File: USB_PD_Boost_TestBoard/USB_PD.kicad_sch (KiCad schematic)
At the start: 44 parts, among them IC1 CYPD3177-24LQXQ, Q1 SI7997DP-T1-GE3, Q2 SI7997DP-T1-GE3, Q3 IRLML0030

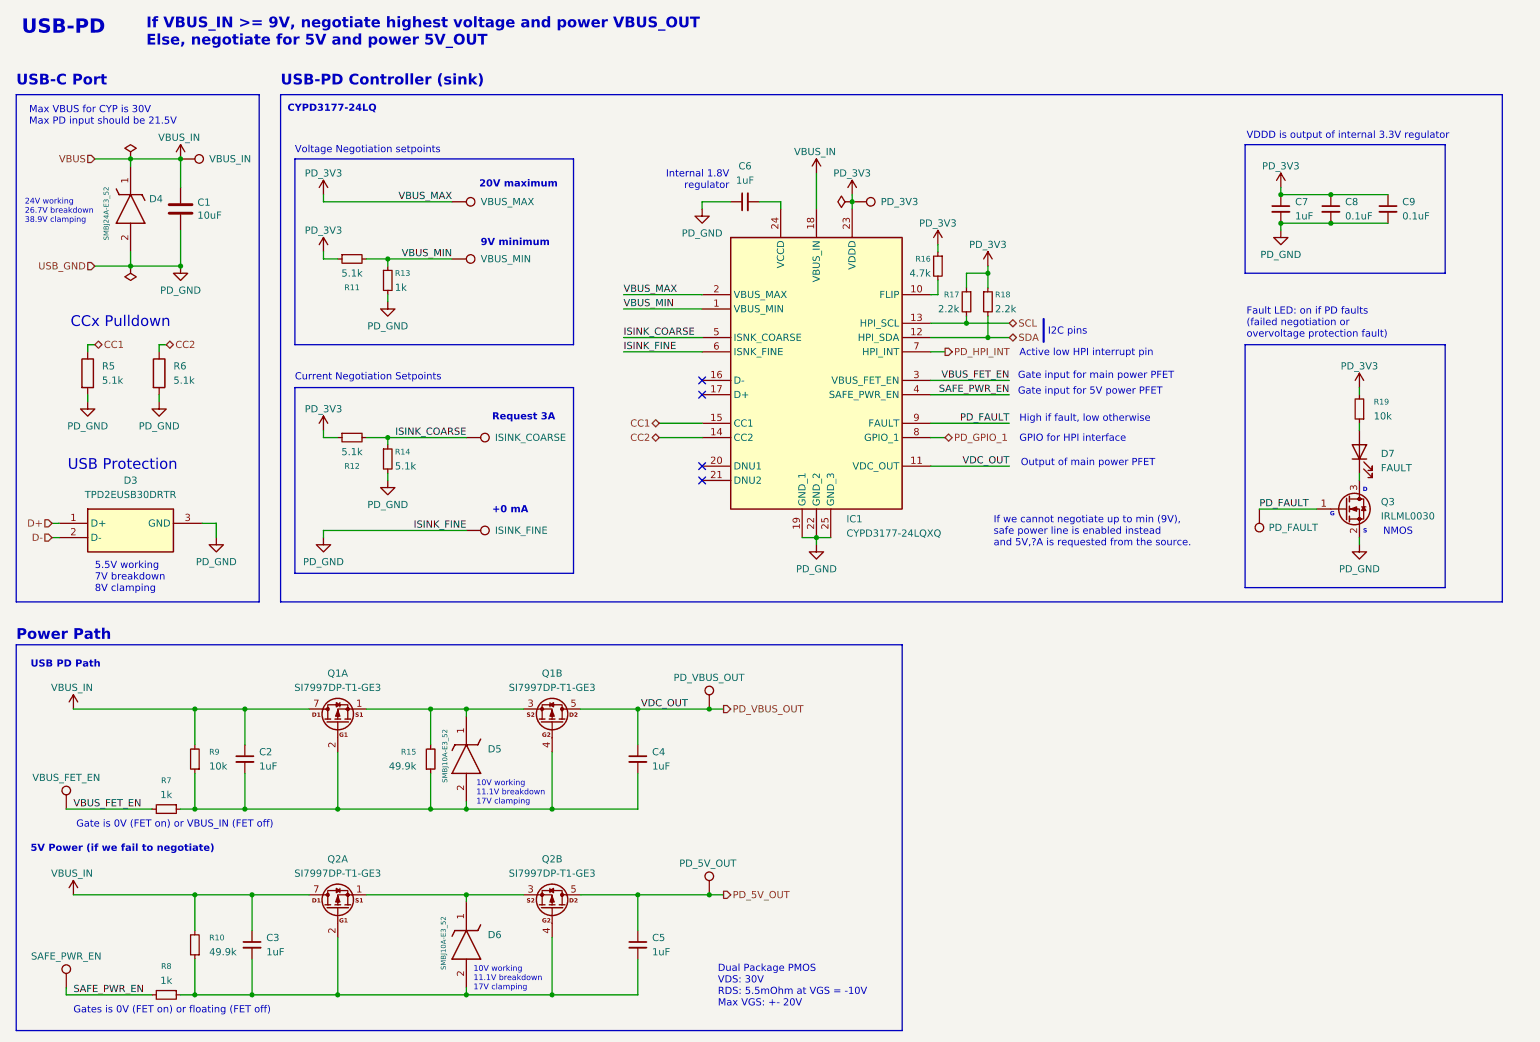
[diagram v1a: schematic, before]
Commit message: addressed comments, changed PD block a little
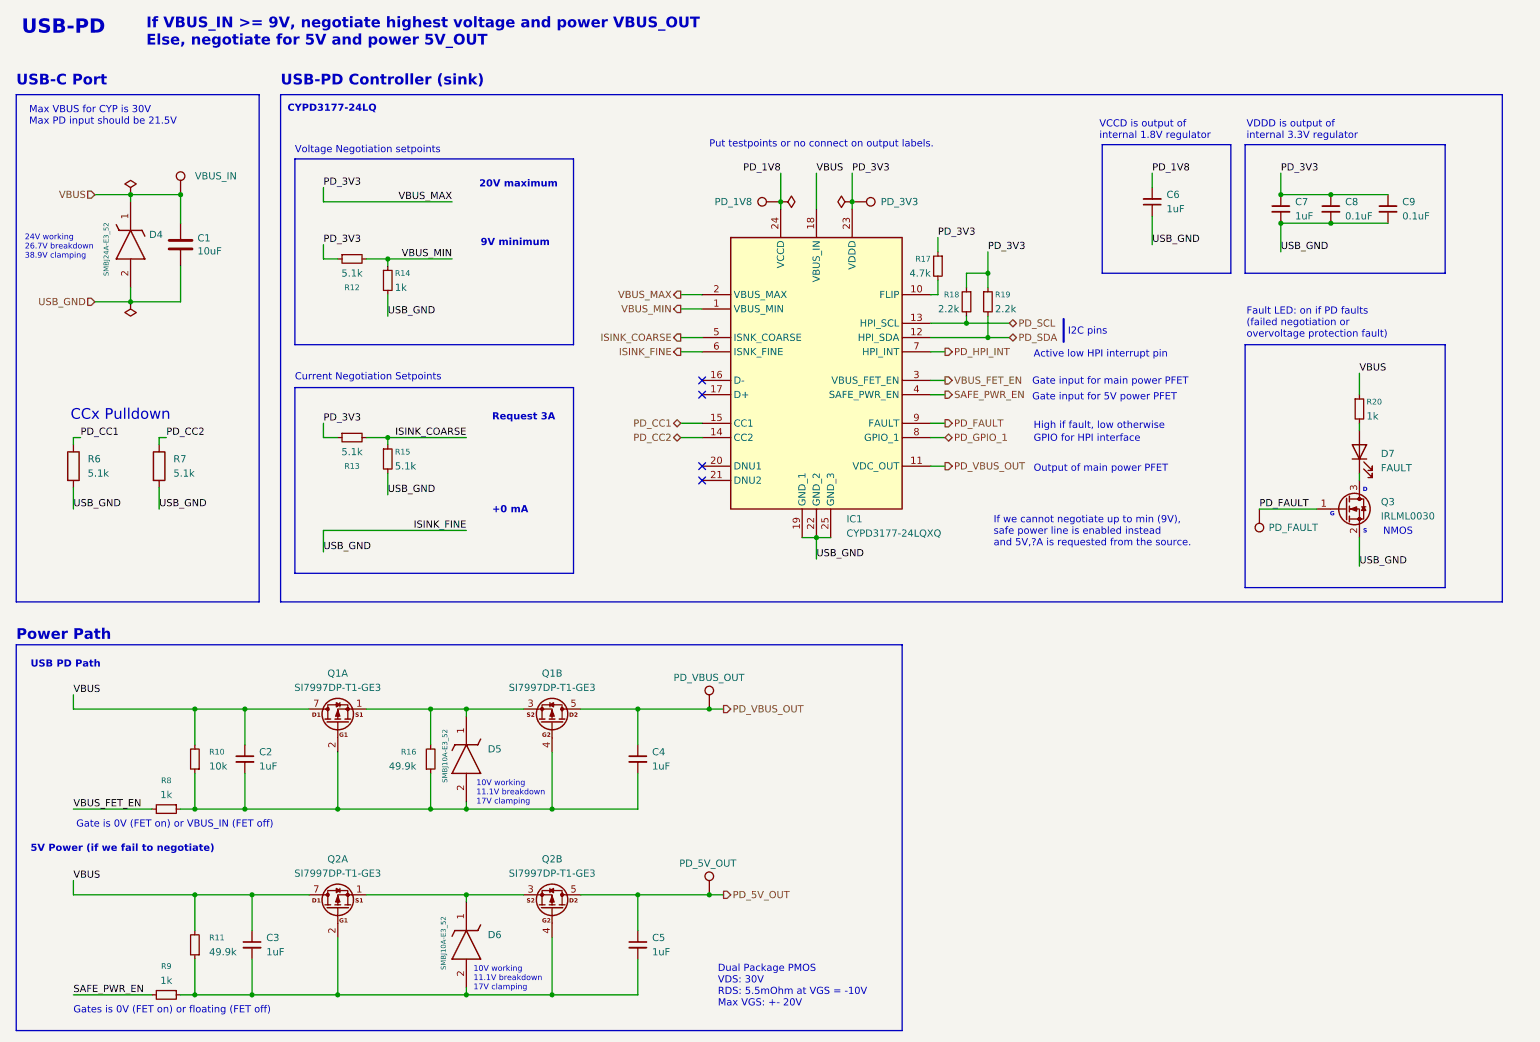
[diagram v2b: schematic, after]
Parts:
- removed D3: TPD2EUSB30DRTR, UTSVT_ICs:TPD2EUSB30DRTR, symbol UTSVT_ICs:TPD2EUSB30DRTR
- removed R19: 10k, Resistor_SMD:R_0603_1608Metric_Pad0.98x0.95mm_HandSolder, symbol Device:R_Small
- removed TP3: VBUS_FET_EN, TestPoint:TestPoint_Pad_1.0x1.0mm, symbol Connector:TestPoint
- removed TP4: SAFE_PWR_EN, TestPoint:TestPoint_Pad_1.0x1.0mm, symbol Connector:TestPoint
- removed TP6: VBUS_MAX, TestPoint:TestPoint_Pad_1.0x1.0mm, symbol Connector:TestPoint
- removed TP7: VBUS_MIN, TestPoint:TestPoint_Pad_1.0x1.0mm, symbol Connector:TestPoint
- removed TP8: ISINK_COARSE, TestPoint:TestPoint_Pad_1.0x1.0mm, symbol Connector:TestPoint
- removed TP9: ISINK_FINE, TestPoint:TestPoint_Pad_1.0x1.0mm, symbol Connector:TestPoint
- added R20: 1k, Resistor_SMD:R_0603_1608Metric_Pad0.98x0.95mm_HandSolder, symbol Device:R_Small
- added TP16: PD_1V8, Connector_PinHeader_2.54mm:PinHeader_1x01_P2.54mm_Vertical, symbol Connector:TestPoint
- D4: symbol UTSVT_Power:SMBJ24A-E3_52 -> utsvt_power:SMBJ24A-E3_52
- D5, D6: symbol UTSVT_Power:SMBJ10A-E3_52 -> utsvt_power:SMBJ10A-E3_52
- IC1: symbol UTSVT_ICs:CYPD3177-24LQXQ -> utsvt_ics:CYPD3177-24LQXQ
- Q1, Q2: symbol UTSVT_ICs:SI7997DP-T1-GE3 -> utsvt_ics:SI7997DP-T1-GE3
- renumbered R9 to R10, R10 to R11, R11 to R12, R12 to R13, R13 to R14, R14 to R15, R15 to R16, R16 to R17, R17 to R18, R18 to R19, R5 to R6, R6 to R7, R7 to R8, R8 to R9, TP5 to TP13, TP10 to TP14, TP11 to TP15, TP12 to TP17, TP13 to TP18
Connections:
- net at D7.2 (A): now also R20.2
- net PD_1V8: now reaches C6.2, IC1.24 (VCCD)
- net PD_1V8: now also TP16.1
- net CC1 renamed PD_CC1
- net CC2 renamed PD_CC2
- net PD_3V3 renamed VBUS_MAX
- net PD_GND renamed ISINK_FINE
- net SCL renamed PD_SCL
- net SDA renamed PD_SDA
- net VBUS_IN renamed VBUS
- net VBUS: now also R20.1
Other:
- note added: "Put testpoints or no connect on output labels."
- note added: "VCCD is output of internal 1.8V regulator"
- note removed: "5.5V working 7V breakdown 8V clamping"
- note removed: "Internal 1.8V regulator"
- note removed: "USB Protection"
- moved on the sheet: C1, C6, D4, R6, R7

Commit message: comments, load resistors, stuff idk
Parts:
- renumbered R9 to R10, R10 to R11, R11 to R12, R12 to R13, R13 to R14, R14 to R15, R15 to R16, R16 to R17, R17 to R18, R18 to R19, R19 to R20, R20 to R21, R6 to R7, R7 to R8, R8 to R9
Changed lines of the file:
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@@
 		(on_board yes)
 		(dnp no)
-		(property "Reference" "R20"
+		(property "Reference" "R21"
 			(at 255.27 83.82 0)
 			(effects
@@
 			(project "USB_PD_Boost_TestBoard"
 				(path "/b6f029de-c5f9-47ba-bc2f-f9cf5cd6ec8c/cc525944-29a1-46f1-9bbd-0373fa6d1795"
-					(reference "R20")
+					(reference "R21")
 					(unit 1)
 				)
@@
 		(on_board yes)
 		(dnp no)
-		(property "Reference" "R10"
+		(property "Reference" "R11"
 			(at 49.53 146.0499 0)
 			(effects
@@
 			(project "USB_PD"
 				(path "/b6f029de-c5f9-47ba-bc2f-f9cf5cd6ec8c/cc525944-29a1-46f1-9bbd-0373fa6d1795"
-					(reference "R10")
+					(reference "R11")
 					(unit 1)
 				)
@@
 		(dnp no)
 		(fields_autoplaced yes)
-		(property "Reference" "R7"
+		(property "Reference" "R8"
 			(at 43.18 93.9799 0)
 			(effects
@@
 			(project "USB_PD"
 				(path "/b6f029de-c5f9-47ba-bc2f-f9cf5cd6ec8c/cc525944-29a1-46f1-9bbd-0373fa6d1795"
-					(reference "R7")
+					(reference "R8")
 					(unit 1)
 				)
@@
 		(dnp no)
 		(fields_autoplaced yes)
-		(property "Reference" "R9"
+		(property "Reference" "R10"
 			(at 41.91 184.15 90)
 			(effects
@@
 			(project "USB_PD"
 				(path "/b6f029de-c5f9-47ba-bc2f-f9cf5cd6ec8c/cc525944-29a1-46f1-9bbd-0373fa6d1795"
-					(reference "R9")
+					(reference "R10")
 					(unit 1)
 				)
@@
 		(on_board yes)
 		(dnp no)
-		(property "Reference" "R14"
+		(property "Reference" "R15"
 			(at 82.55 60.96 0)
 			(effects
@@
 			(project "USB_PD"
 				(path "/b6f029de-c5f9-47ba-bc2f-f9cf5cd6ec8c/cc525944-29a1-46f1-9bbd-0373fa6d1795"
-					(reference "R14")
+					(reference "R15")
 					(unit 1)
 				)
@@
 		(on_board yes)
 		(dnp no)
-		(property "Reference" "R17"
+		(property "Reference" "R18"
 			(at 177.8 58.42 0)
 			(effects
@@
 			(project "USB_PD"
 				(path "/b6f029de-c5f9-47ba-bc2f-f9cf5cd6ec8c/cc525944-29a1-46f1-9bbd-0373fa6d1795"
-					(reference "R17")
+					(reference "R18")
 					(unit 1)
 				)
@@
 		(on_board yes)
 		(dnp no)
-		(property "Reference" "R19"
+		(property "Reference" "R20"
 			(at 189.23 64.77 0)
 			(effects
@@
 			(project "USB_PD"
 				(path "/b6f029de-c5f9-47ba-bc2f-f9cf5cd6ec8c/cc525944-29a1-46f1-9bbd-0373fa6d1795"
-					(reference "R19")
+					(reference "R20")
 					(unit 1)
 				)
@@
 		(on_board yes)
 		(dnp no)
-		(property "Reference" "R15"
+		(property "Reference" "R16"
 			(at 82.55 92.71 0)
 			(effects
@@
 			(project "USB_PD"
 				(path "/b6f029de-c5f9-47ba-bc2f-f9cf5cd6ec8c/cc525944-29a1-46f1-9bbd-0373fa6d1795"
-					(reference "R15")
+					(reference "R16")
 					(unit 1)
 				)
@@
 		(on_board yes)
 		(dnp no)
-		(property "Reference" "R12"
+		(property "Reference" "R13"
 			(at 74.93 63.5 90)
 			(effects
@@
 			(project ""
 				(path "/b6f029de-c5f9-47ba-bc2f-f9cf5cd6ec8c/cc525944-29a1-46f1-9bbd-0373fa6d1795"
-					(reference "R12")
+					(reference "R13")
 					(unit 1)
 				)
@@
 		(on_board yes)
 		(dnp no)
-		(property "Reference" "R18"
+		(property "Reference" "R19"
 			(at 182.88 64.77 0)
 			(effects
@@
 			(project "USB_PD"
 				(path "/b6f029de-c5f9-47ba-bc2f-f9cf5cd6ec8c/cc525944-29a1-46f1-9bbd-0373fa6d1795"
-					(reference "R18")
+					(reference "R19")
 					(unit 1)
 				)
@@
 		(dnp no)
 		(fields_autoplaced yes)
-		(property "Reference" "R8"
+		(property "Reference" "R9"
 			(at 41.91 151.13 90)
 			(effects
@@
 			(project "USB_PD"
 				(path "/b6f029de-c5f9-47ba-bc2f-f9cf5cd6ec8c/cc525944-29a1-46f1-9bbd-0373fa6d1795"
-					(reference "R8")
+					(reference "R9")
 					(unit 1)
 				)
@@
 		(dnp no)
 		(fields_autoplaced yes)
-		(property "Reference" "R6"
+		(property "Reference" "R7"
 			(at 27.94 93.9799 0)
 			(effects
@@
 			(project "USB_PD"
 				(path "/b6f029de-c5f9-47ba-bc2f-f9cf5cd6ec8c/cc525944-29a1-46f1-9bbd-0373fa6d1795"
-					(reference "R6")
+					(reference "R7")
 					(unit 1)
 				)
@@
 		(dnp no)
 		(fields_autoplaced yes)
-		(property "Reference" "R11"
+		(property "Reference" "R12"
 			(at 49.53 179.0699 0)
 			(effects
@@
 			(project "USB_PD"
 				(path "/b6f029de-c5f9-47ba-bc2f-f9cf5cd6ec8c/cc525944-29a1-46f1-9bbd-0373fa6d1795"
-					(reference "R11")
+					(reference "R12")
 					(unit 1)
 				)
@@
 		(on_board yes)
 		(dnp no)
-		(property "Reference" "R16"
+		(property "Reference" "R17"
 			(at 86.36 146.0499 0)
 			(effects
@@
 			(project "USB_PD"
 				(path "/b6f029de-c5f9-47ba-bc2f-f9cf5cd6ec8c/cc525944-29a1-46f1-9bbd-0373fa6d1795"
-					(reference "R16")
+					(reference "R17")
 					(unit 1)
 				)
@@
 		(on_board yes)
 		(dnp no)
-		(property "Reference" "R13"
+		(property "Reference" "R14"
 			(at 74.93 95.25 90)
 			(effects
@@
 			(project "USB_PD"
 				(path "/b6f029de-c5f9-47ba-bc2f-f9cf5cd6ec8c/cc525944-29a1-46f1-9bbd-0373fa6d1795"
-					(reference "R13")
+					(reference "R14")
 					(unit 1)
 				)

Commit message: son
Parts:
- renumbered TP13 to TP15, TP14 to TP16, TP15 to TP17, TP16 to TP18, TP17 to TP19, TP18 to TP20
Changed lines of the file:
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@@
 		(on_board yes)
 		(dnp no)
-		(property "Reference" "TP18"
+		(property "Reference" "TP20"
 			(at 238.76 104.9019 0)
 			(effects
@@
 			(project "USB_PD"
 				(path "/b6f029de-c5f9-47ba-bc2f-f9cf5cd6ec8c/cc525944-29a1-46f1-9bbd-0373fa6d1795"
-					(reference "TP18")
+					(reference "TP20")
 					(unit 1)
 				)
@@
 		(on_board yes)
 		(dnp no)
-		(property "Reference" "TP15"
+		(property "Reference" "TP17"
 			(at 135.89 169.4181 0)
 			(effects
@@
 			(project "USB_PD"
 				(path "/b6f029de-c5f9-47ba-bc2f-f9cf5cd6ec8c/cc525944-29a1-46f1-9bbd-0373fa6d1795"
-					(reference "TP15")
+					(reference "TP17")
 					(unit 1)
 				)
@@
 		(on_board yes)
 		(dnp no)
-		(property "Reference" "TP14"
+		(property "Reference" "TP16"
 			(at 135.89 136.3981 0)
 			(effects
@@
 			(project "USB_PD"
 				(path "/b6f029de-c5f9-47ba-bc2f-f9cf5cd6ec8c/cc525944-29a1-46f1-9bbd-0373fa6d1795"
-					(reference "TP14")
+					(reference "TP16")
 					(unit 1)
 				)
@@
 		(dnp no)
 		(fields_autoplaced yes)
-		(property "Reference" "TP13"
+		(property "Reference" "TP15"
 			(at 41.91 44.9581 0)
 			(effects
@@
 			(project "USB_PD"
 				(path "/b6f029de-c5f9-47ba-bc2f-f9cf5cd6ec8c/cc525944-29a1-46f1-9bbd-0373fa6d1795"
-					(reference "TP13")
+					(reference "TP15")
 					(unit 1)
 				)
@@
 		(on_board yes)
 		(dnp no)
-		(property "Reference" "TP17"
+		(property "Reference" "TP19"
 			(at 165.8619 45.72 0)
 			(effects
@@
 			(project "USB_PD"
 				(path "/b6f029de-c5f9-47ba-bc2f-f9cf5cd6ec8c/cc525944-29a1-46f1-9bbd-0373fa6d1795"
-					(reference "TP17")
+					(reference "TP19")
 					(unit 1)
 				)
@@
 		(on_board yes)
 		(dnp no)
-		(property "Reference" "TP16"
+		(property "Reference" "TP18"
 			(at 149.0981 50.8 0)
 			(effects
@@
 			(project "USB_PD_Boost_TestBoard"
 				(path "/b6f029de-c5f9-47ba-bc2f-f9cf5cd6ec8c/cc525944-29a1-46f1-9bbd-0373fa6d1795"
-					(reference "TP16")
-					(unit 1)
-				)
+					(reference "TP18")
+					(unit 1)
+				)

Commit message: something
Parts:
- TP20: footprint TestPoint:TestPoint_Pad_1.0x1.0mm -> Connector_PinHeader_2.54mm:PinHeader_1x01_P2.54mm_Vertical
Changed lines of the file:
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@@
 			)
 		)
-		(property "Footprint" "TestPoint:TestPoint_Pad_1.0x1.0mm"
+		(property "Footprint" "Connector_PinHeader_2.54mm:PinHeader_1x01_P2.54mm_Vertical"
 			(at 231.14 102.87 0)
 			(effects
